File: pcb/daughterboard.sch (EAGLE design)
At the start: 26 parts, among them IC3 STM32F042F4, SW1 324_SW, SW2 324_SW, SW3 324_SW, SW4 324_SW, SW5 324_SW, SW6 324_SW, U4 XC6206_DEV

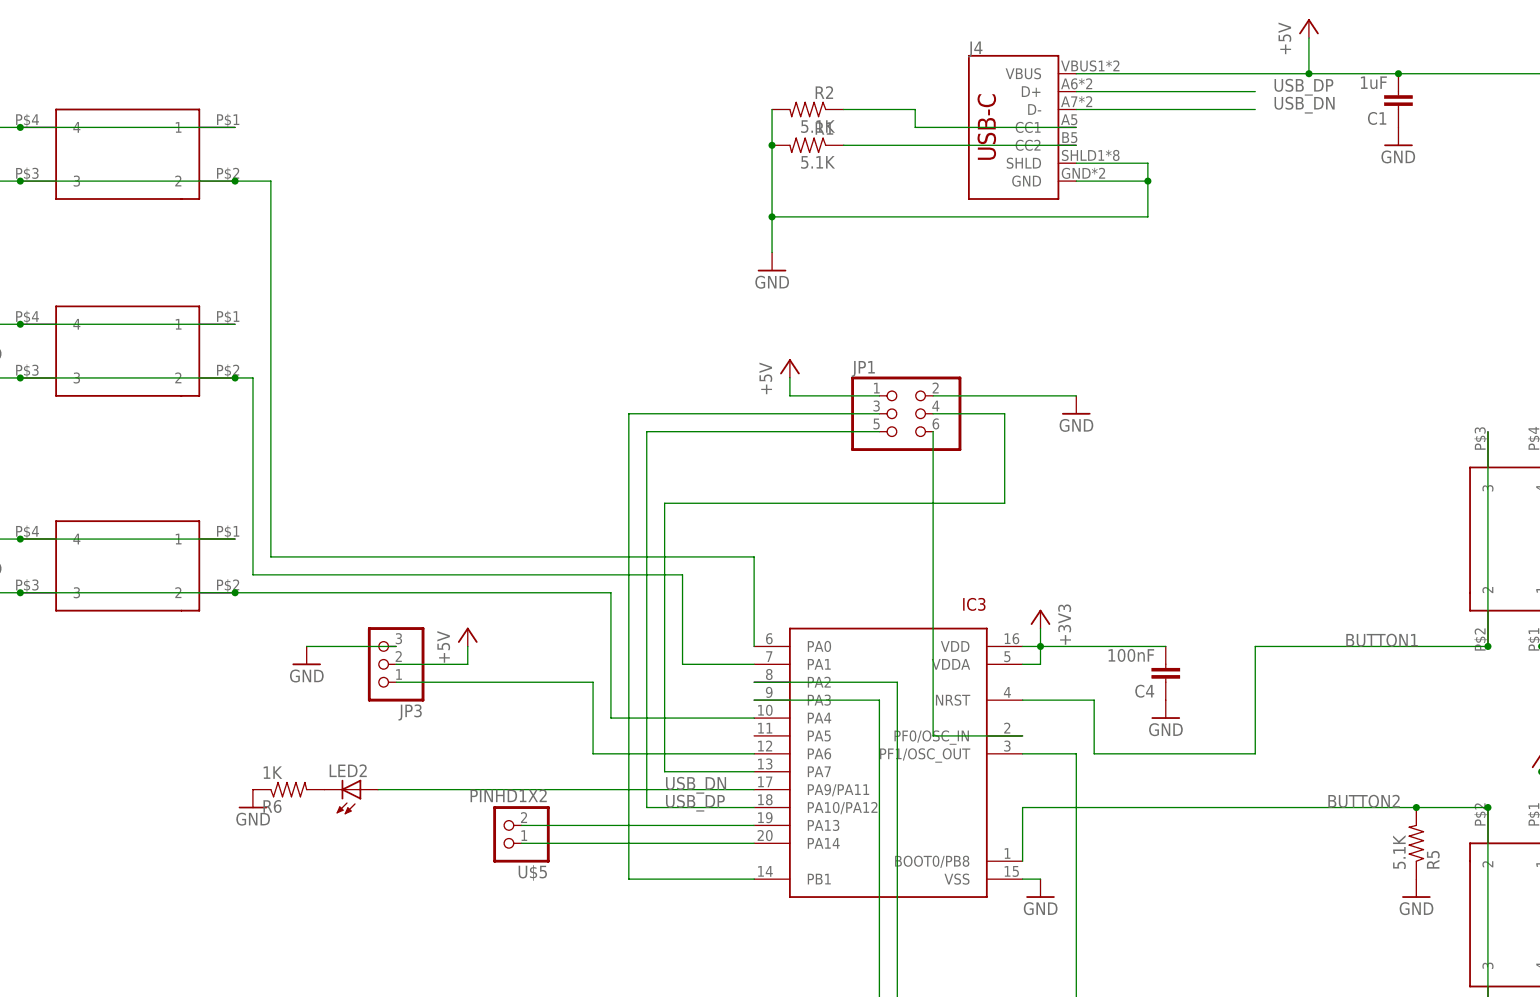
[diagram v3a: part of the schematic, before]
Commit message: added pullup on 1wire, gnd pour cleanup
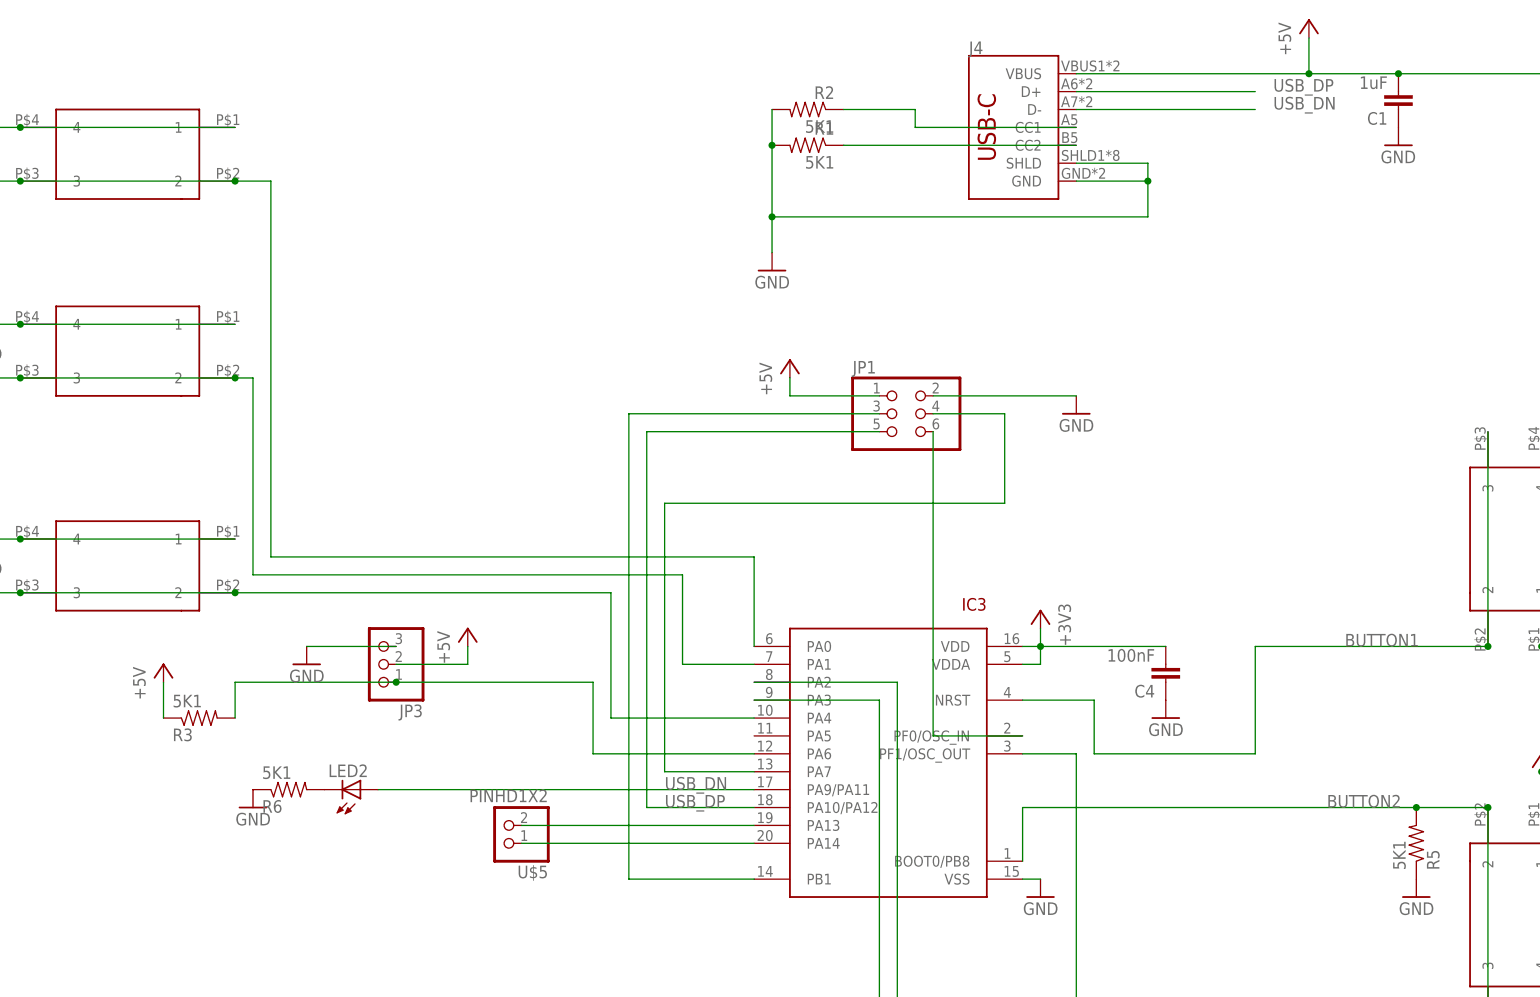
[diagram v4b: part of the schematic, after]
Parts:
- added R3: 5K1, SparkFun-Passives:RESISTOR0805-RES
- R1, R2, R5: value 5.1K -> 5K1
- R6: value 1K -> 5K1
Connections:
- net +5V: now also R3.1
- net N$5: now also R3.2
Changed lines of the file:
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@@
 <part name="+3V5" library="supply1" library_urn="urn:adsk.eagle:library:371" deviceset="+3V3" device=""/>
 <part name="GND6" library="supply1" deviceset="GND" device=""/>
-<part name="R1" library="joyAnalog" deviceset="RESISTOR" device="0805-RES" value="5.1K"/>
-<part name="R2" library="joyAnalog" deviceset="RESISTOR" device="0805-RES" value="5.1K"/>
+<part name="R1" library="joyAnalog" deviceset="RESISTOR" device="0805-RES" value="5K1"/>
+<part name="R2" library="joyAnalog" deviceset="RESISTOR" device="0805-RES" value="5K1"/>
 <part name="C1" library="clock" deviceset="CAP" device="0805" value="1uF"/>
 <part name="GND16" library="supply1" library_urn="urn:adsk.eagle:library:371" deviceset="GND" device=""/>
@@
 <part name="SW4" library="3pos_slide_switch_centered" deviceset="324_SW" device="" value="324_SW"/>
 <part name="LED2" library="adafruit" deviceset="LED" device="CHIP-LED0805"/>
-<part name="R6" library="SparkFun-Passives" deviceset="RESISTOR" device="0805-RES" value="1K"/>
+<part name="R6" library="SparkFun-Passives" deviceset="RESISTOR" device="0805-RES" value="5K1"/>
 <part name="GND9" library="backplane" deviceset="GND" device=""/>
 <part name="+3V2" library="supply1" library_urn="urn:adsk.eagle:library:371" deviceset="+3V3" device=""/>
-<part name="R5" library="joyAnalog" deviceset="RESISTOR" device="0805-RES" value="5.1K"/>
+<part name="R5" library="joyAnalog" deviceset="RESISTOR" device="0805-RES" value="5K1"/>
 <part name="GND10" library="supply1" deviceset="GND" device=""/>
 <part name="U4" library="3pos_slide_switch" deviceset="XC6206_DEV" device=""/>
@@
 <part name="U$7" library="adafruit_changed" deviceset="PINHD1X2" device=""/>
 <part name="GND14" library="supply1" deviceset="GND" device=""/>
+<part name="P+4" library="supply1" library_urn="urn:adsk.eagle:library:371" deviceset="+5V" device=""/>
+<part name="R3" library="SparkFun-Passives" deviceset="RESISTOR" device="0805-RES" value="5K1"/>
 </parts>
 <sheets>
@@
 <instance part="GND14" gate="1" x="63.5" y="-55.88" smashed="yes" rot="MR0">
 <attribute name="VALUE" x="66.04" y="-58.42" size="1.778" layer="96" rot="MR0"/>
+</instance>
+<instance part="P+4" gate="1" x="-101.6" y="38.1" smashed="yes">
+<attribute name="VALUE" x="-104.14" y="33.02" size="1.778" layer="96" rot="R90"/>
+</instance>
+<instance part="R3" gate="G$1" x="-96.52" y="30.48" smashed="yes" rot="MR180">
+<attribute name="NAME" x="-100.33" y="28.9814" size="1.778" layer="95" rot="MR180"/>
+<attribute name="VALUE" x="-100.33" y="33.782" size="1.778" layer="96" rot="MR180"/>
 </instance>
 </instances>
@@
 <wire x1="-58.42" y1="38.1" x2="-58.42" y2="40.64" width="0.1524" layer="91"/>
 </segment>
+<segment>
+<pinref part="R3" gate="G$1" pin="1"/>
+<pinref part="P+4" gate="1" pin="+5V"/>
+<wire x1="-101.6" y1="30.48" x2="-101.6" y2="35.56" width="0.1524" layer="91"/>
+</segment>
 </net>
 <net name="BUTTON1" class="0">
@@
 <pinref part="IC3" gate="G$1" pin="PA6"/>
 <wire x1="-40.64" y1="25.4" x2="-17.78" y2="25.4" width="0.1524" layer="91"/>
-</segment>
-</net>
+<wire x1="-68.58" y1="35.56" x2="-91.44" y2="35.56" width="0.1524" layer="91"/>
+<wire x1="-91.44" y1="35.56" x2="-91.44" y2="30.48" width="0.1524" layer="91"/>
+<junction x="-68.58" y="35.56"/>
+<pinref part="R3" gate="G$1" pin="2"/>
+</segment>
+</net>

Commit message: cleanup
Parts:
- removed SW3: 324_SW, 3pos_slide_switch_centered:324_SW
- added U$8: PINHD1X2, adafruit_changed:PINHD1X2
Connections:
- net BUTTON1: now also U$8.1; no longer SW3.2, SW3.3
- net GND: now also U$8.2; no longer SW3.1, SW3.4
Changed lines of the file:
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@@
 <part name="GND8" library="supply1" deviceset="GND" device=""/>
 <part name="GND11" library="supply1" library_urn="urn:adsk.eagle:library:371" deviceset="GND" device=""/>
-<part name="SW3" library="3pos_slide_switch_centered" deviceset="324_SW" device="" value="324_SW"/>
 <part name="SW4" library="3pos_slide_switch_centered" deviceset="324_SW" device="" value="324_SW"/>
 <part name="LED2" library="adafruit" deviceset="LED" device="CHIP-LED0805"/>
@@
 <part name="P+4" library="supply1" library_urn="urn:adsk.eagle:library:371" deviceset="+5V" device=""/>
 <part name="R3" library="SparkFun-Passives" deviceset="RESISTOR" device="0805-RES" value="5K1"/>
+<part name="U$8" library="adafruit_changed" deviceset="PINHD1X2" device=""/>
 </parts>
 <sheets>
@@
 <attribute name="VALUE" x="109.22" y="35.56" size="1.778" layer="96"/>
 </instance>
-<instance part="SW3" gate="G$1" x="91.44" y="55.88" smashed="yes" rot="R90"/>
 <instance part="SW4" gate="G$1" x="91.44" y="2.54" smashed="yes" rot="MR270"/>
 <instance part="LED2" gate="G$1" x="-73.66" y="20.32" smashed="yes" rot="MR90">
@@
 <attribute name="NAME" x="-100.33" y="28.9814" size="1.778" layer="95" rot="MR180"/>
 <attribute name="VALUE" x="-100.33" y="33.782" size="1.778" layer="96" rot="MR180"/>
+</instance>
+<instance part="U$8" gate="1" x="91.44" y="83.82" smashed="yes" rot="R90">
+<attribute name="NAME" x="85.725" y="77.47" size="1.778" layer="95" rot="R90"/>
+<attribute name="VALUE" x="96.52" y="77.47" size="1.778" layer="96" rot="R90"/>
 </instance>
 </instances>
@@
 <segment>
 <pinref part="GND11" gate="1" pin="GND"/>
-<pinref part="SW3" gate="G$1" pin="1"/>
 <wire x1="93.98" y1="40.64" x2="111.76" y2="40.64" width="0.1524" layer="91"/>
-<pinref part="SW3" gate="G$1" pin="4"/>
 <wire x1="93.98" y1="71.12" x2="93.98" y2="40.64" width="0.1524" layer="91"/>
-<junction x="93.98" y="40.64"/>
+<pinref part="U$8" gate="1" pin="2"/>
+<wire x1="93.98" y1="71.12" x2="91.44" y2="71.12" width="0.1524" layer="91"/>
+<wire x1="91.44" y1="71.12" x2="91.44" y2="81.28" width="0.1524" layer="91"/>
 </segment>
 <segment>
@@
 <segment>
 <label x="66.04" y="40.64" size="1.778" layer="95"/>
-<pinref part="SW3" gate="G$1" pin="2"/>
 <wire x1="53.34" y1="40.64" x2="86.36" y2="40.64" width="0.1524" layer="91"/>
-<pinref part="SW3" gate="G$1" pin="3"/>
 <wire x1="86.36" y1="71.12" x2="86.36" y2="40.64" width="0.1524" layer="91"/>
-<junction x="86.36" y="40.64"/>
 <pinref part="IC3" gate="G$1" pin="NRST"/>
 <wire x1="20.32" y1="33.02" x2="30.48" y2="33.02" width="0.1524" layer="91"/>
@@
 <wire x1="30.48" y1="25.4" x2="53.34" y2="25.4" width="0.1524" layer="91"/>
 <wire x1="53.34" y1="25.4" x2="53.34" y2="40.64" width="0.1524" layer="91"/>
-</segment>
-</net>
+<pinref part="U$8" gate="1" pin="1"/>
+<wire x1="86.36" y1="71.12" x2="88.9" y2="71.12" width="0.1524" layer="91"/>
+<wire x1="88.9" y1="71.12" x2="88.9" y2="81.28" width="0.1524" layer="91"/>
+</segment>
+</net>

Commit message: finishing touches before production run
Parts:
- removed SW6: 324_SW, 3pos_slide_switch_centered:324_SW
- added SW3: 324_SW, 3pos_slide_switch_centered:324_SW
- C1, C2: value 1uF -> 2.2uF
- renumbered C4 to C3, IC3 to IC1, J4 to J1, JP3 to JP2, LED2 to LED1, R6 to R4, U4 to U1
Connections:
- net +3V3: now also U$7.1; no longer U$4.1
- net BUTTON1: now also U$3.1; no longer U$8.1
- net BUTTON2: now also U$7.2; no longer U$4.2
- net GND: now also SW3.1, SW3.4, SW5.2, SW5.3, U$4.2, U$8.1; no longer SW5.1, SW5.4, SW6.2, SW6.3, U$7.1, U$8.2
- net N$11: now also SW1.2, SW1.3, U$1.1; no longer SW5.2, SW5.3, U$3.1
- net N$12: now also SW5.1, SW5.4, U$8.2; no longer SW6.1, SW6.4, U$7.2
- net N$31: now also R2.1; no longer R1.1
- net N$33: now also R1.1; no longer R2.1
- net N$9: now also SW3.2, SW3.3, U$4.1; no longer SW1.2, SW1.3, U$1.1
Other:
- moved on the sheet: R1, R2, U$1, U$3, U$4, U$7, U$8
